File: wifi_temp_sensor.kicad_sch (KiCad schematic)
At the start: 9 parts, among them J1 USB_B_Mini, J2 Conn_02x04_Odd_Even, J3 Conn_01x04, J4 Conn_01x06, J6 Conn_01x01, J8 Conn_01x01, SW1 SW_DIP_x01

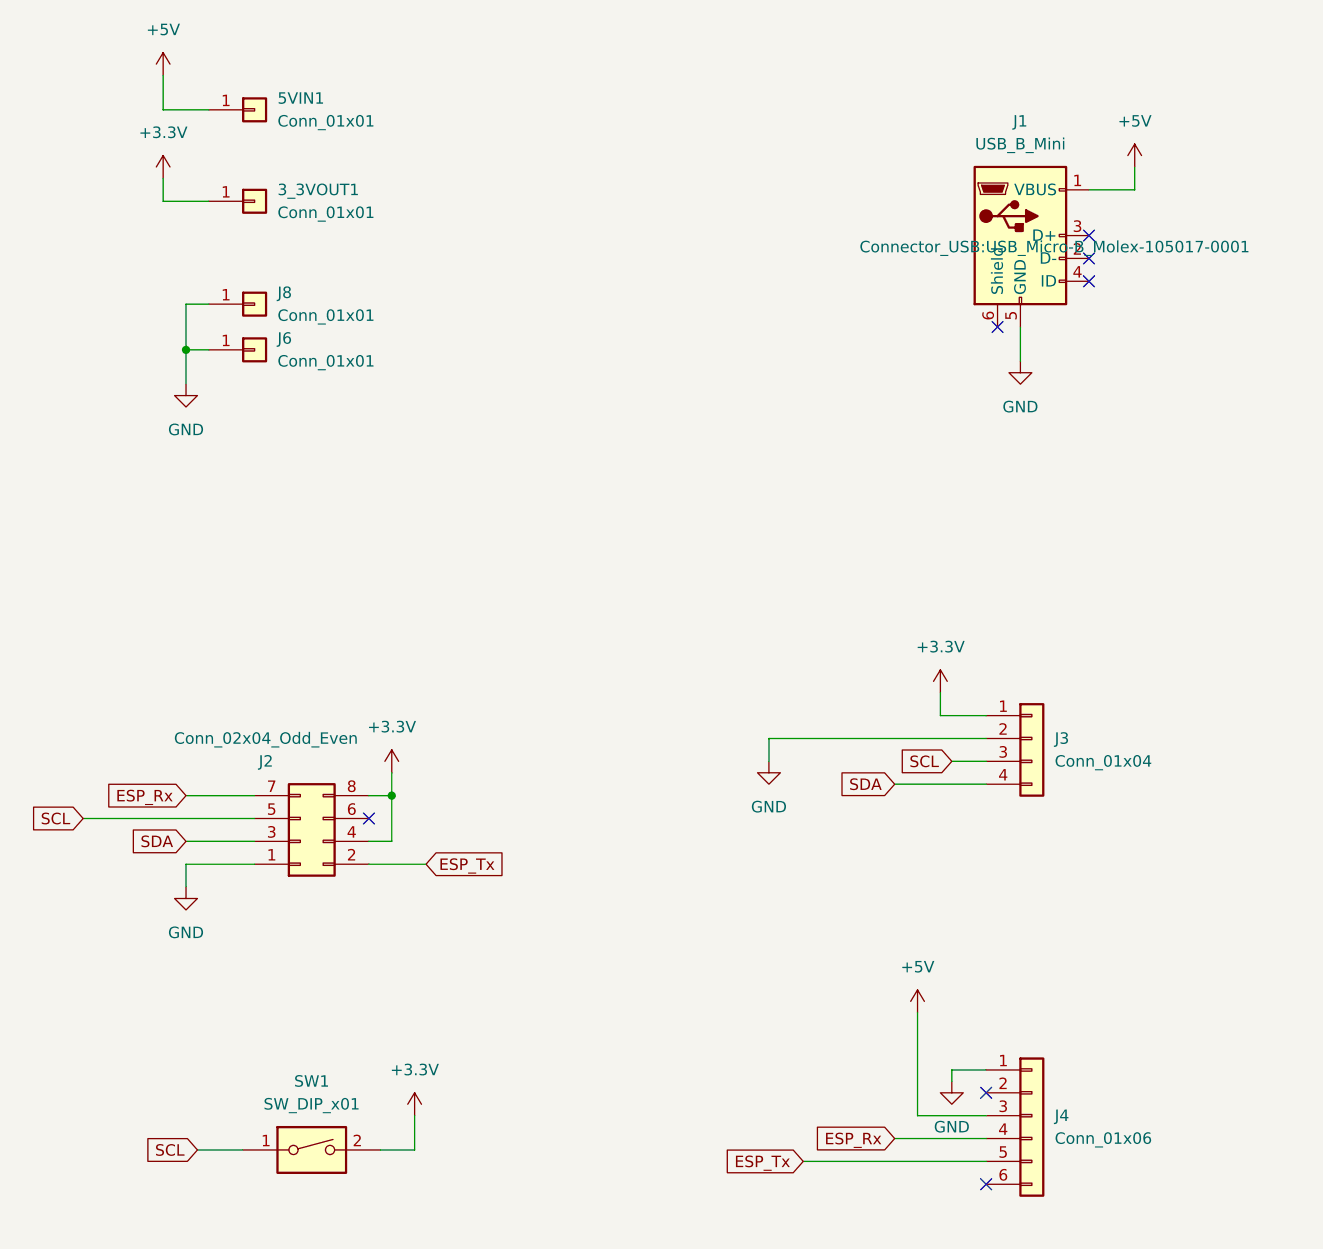
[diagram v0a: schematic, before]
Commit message: Fixed minor issues and re-did the PCB
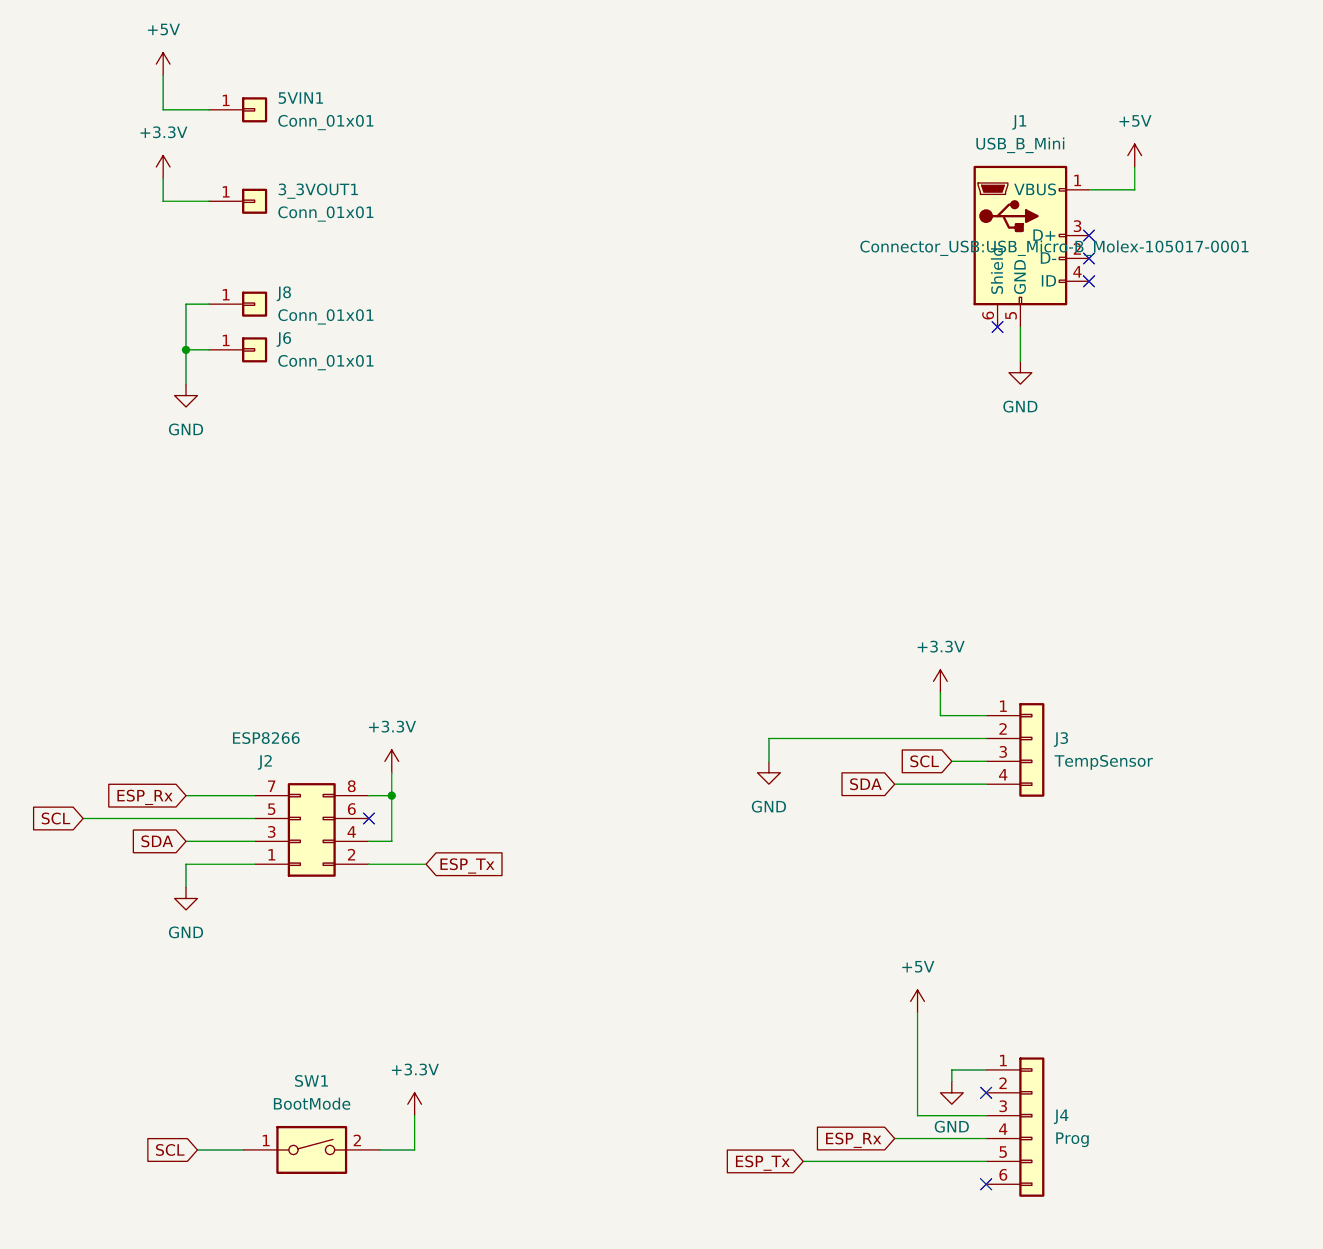
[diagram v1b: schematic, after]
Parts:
- J2: value Conn_02x04_Odd_Even -> ESP8266
- J3: value Conn_01x04 -> TempSensor
- J4: value Conn_01x06 -> Prog
- SW1: value SW_DIP_x01 -> BootMode
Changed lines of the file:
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@@
       (effects (font (size 1.27 1.27)))
     )
-    (property "Value" "SW_DIP_x01" (at 167.64 148.59 0)
+    (property "Value" "BootMode" (at 167.64 148.59 0)
       (effects (font (size 1.27 1.27)))
     )
@@
       (effects (font (size 1.27 1.27)) (justify left))
     )
-    (property "Value" "Conn_01x04" (at 250.19 110.49 0)
+    (property "Value" "TempSensor" (at 250.19 110.49 0)
       (effects (font (size 1.27 1.27)) (justify left))
     )
@@
       (effects (font (size 1.27 1.27)) (justify left))
     )
-    (property "Value" "Conn_01x06" (at 250.19 152.4 0)
+    (property "Value" "Prog" (at 250.19 152.4 0)
       (effects (font (size 1.27 1.27)) (justify left))
     )
@@
       (effects (font (size 1.27 1.27)))
     )
-    (property "Value" "Conn_02x04_Odd_Even" (at 162.56 107.95 0)
-      (effects (font (size 1.27 1.27)))
-    )
+    (property "Value" "ESP8266" (at 162.56 107.95 0)
+      (effects (font (size 1.27 1.27)))
+    )

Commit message: Resized board and added LDO PSU
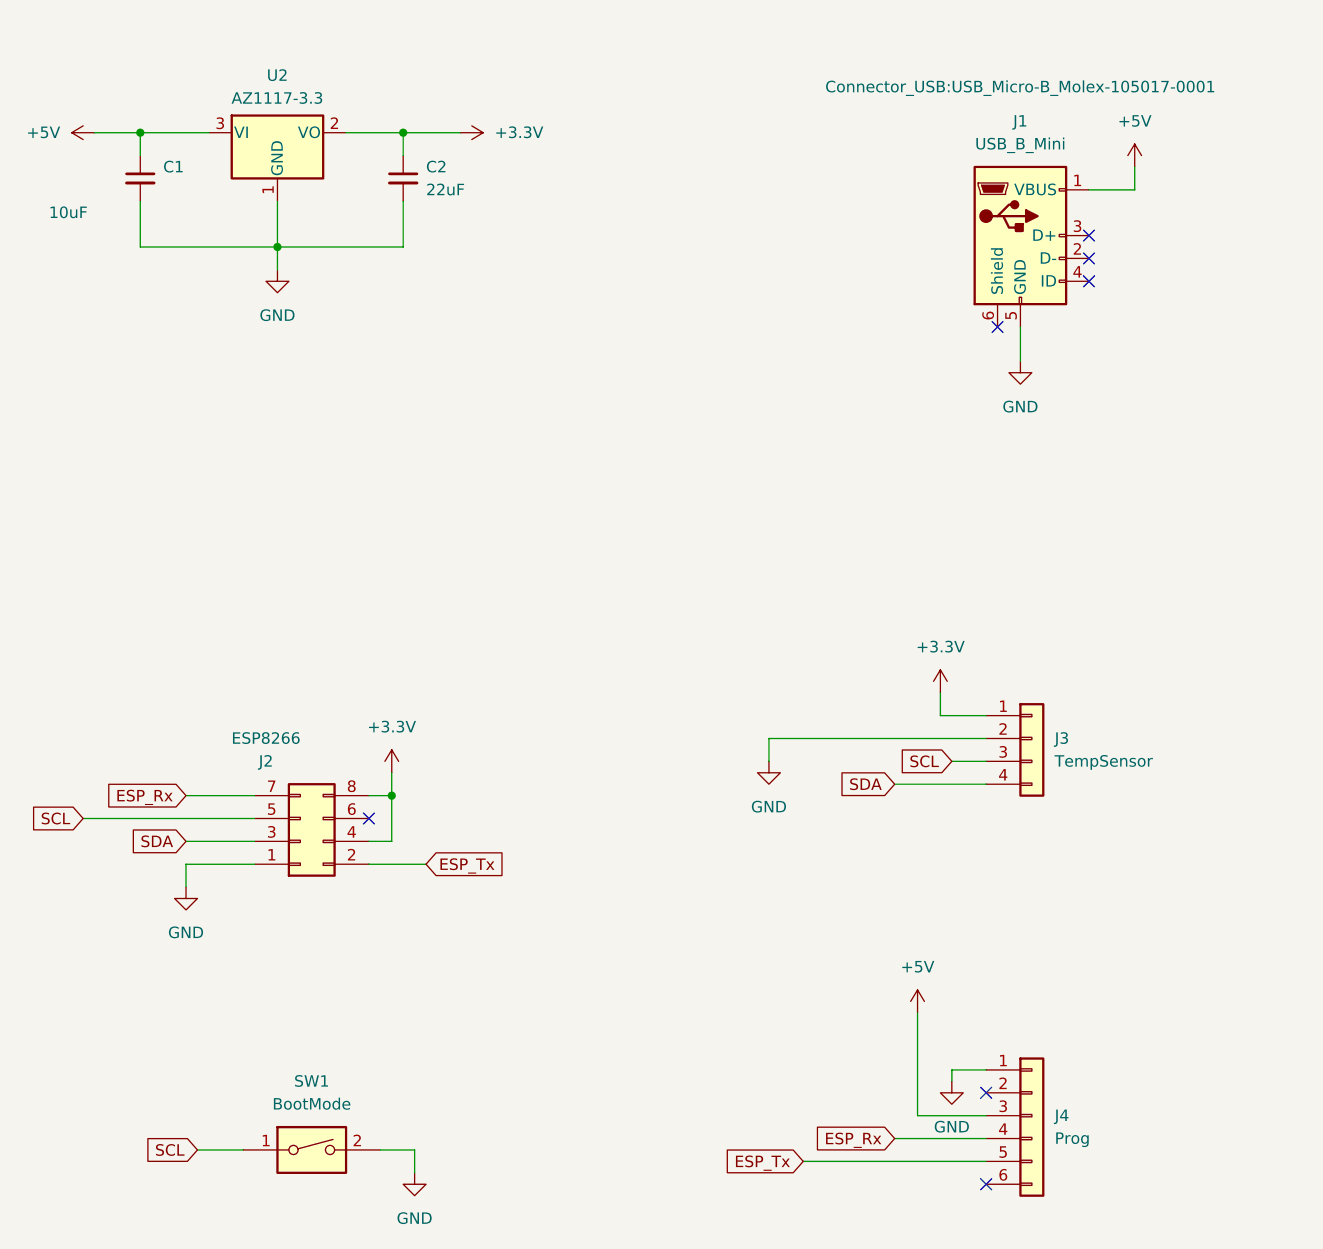
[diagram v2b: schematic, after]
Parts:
- removed 3_3VOUT1, 5VIN1, J6, J8: Conn_01x01, Connector_PinSocket_2.54mm:PinSocket_1x01_P2.54mm_Vertical, symbol Connector_Generic:Conn_01x01
- added C1: 10uF, Capacitor_SMD:C_1206_3216Metric, symbol Device:C_Small
- added C2: 22uF, Capacitor_SMD:C_1206_3216Metric, symbol Device:C_Small
- added U2: AZ1117-3.3, Package_TO_SOT_SMD:SOT-89-3, symbol Regulator_Linear:AZ1117-3.3
- J3: footprint Connector_PinSocket_2.54mm:PinSocket_1x04_P2.54mm_Horizontal -> Connector_PinSocket_2.54mm:PinSocket_1x04_P2.54mm_Vertical
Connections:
- net +3.3V: now also C2.1, U2.2 (VO); no longer SW1.2
- net +5V: now also C1.1, U2.3 (VI)
- net GND: now also SW1.2, C1.2, C2.2, U2.1 (GND)
